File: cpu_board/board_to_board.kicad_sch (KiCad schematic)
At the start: 2 parts

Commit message: clean up board2board connector and organize TODOs
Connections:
- net BOOT_MODE1 is gone; now on net GPIO_SNVS_02: J?.21
- net DA_nRESET is gone; now on net GND: J?.59
- net ENET_RGMII_MDIO is gone; now on net GND: J?.46
- net ENET_RGMII_RXC is gone; now on net GPIO_DISP_B2_13: J?.78
- net ENET_RGMII_RXD0 is gone; now on net GPIO_DISP_B2_10: J?.70
- net ENET_RGMII_RXD1 is gone; now on net GPIO_DISP_B2_09: J?.68
- net ENET_RGMII_RXD2 is gone; now on net GPIO_DISP_B2_08: J?.66
- net ENET_RGMII_RXD3 is gone; now on net GND: J?.72
- net ENET_RGMII_RX_EN is gone; now on net GPIO_DISP_B2_12: J?.76
- net ENET_RGMII_TXC is gone; now on net GPIO_EMC_B2_10: J?.65
- net ENET_RGMII_TXD0 is gone; now on net GPIO_EMC_B2_09: J?.61
- net ENET_RGMII_TXD1 is gone; now on net GPIO_EMC_B2_08: J?.59
- net ENET_RGMII_TXD2 is gone; now on net GPIO_EMC_B2_07: J?.57
- net ENET_RGMII_TXD3 is gone; now on net GPIO_EMC_B2_06: J?.55
- net ENET_RGMII_TX_EN is gone; now on net GND: J?.63
- net GPIO_AD_24 is gone; now on net GND: J?.89
- net GPIO_AD_25 is gone; now on net GPIO_AD_27: J?.91
- net GPIO_EMC_B1_40 is gone; now on net VDD_3V3: J?.2
- net GPIO_EMC_B1_41 is gone; now on net GND: J?.22
- net GPIO_LPSR_10 is gone; now on net GND: J?.48
- net GPIO_LPSR_13 is gone; now on net GPIO_AD_07: J?.43
- net GPIO_LPSR_14 is gone; now on net GPIO_AD_06: J?.41
- net GPIO_LPSR_15 is gone; now on net GND: J?.39
- net GPIO_SD_B1_02 is gone; now on net GPIO_AD_34: J?.96
- net GPIO_SD_B2_04 is gone; now on net GND: J?.79
- net MIPI_DSI_D1_N is gone; now on net GND: J?.93
- net MIPI_DSI_D1_P is gone; now on net GND: J?.91
- net VDDA_1P0 is gone; now on net VDD_3V3: J?.5
- net VDD_LPSR_IN is gone; now on net VDD_1V8: J?.13
- net DAC_OUT: now also J?.20; no longer J?.95
- net DCDC_1V8_OUT: no longer J?.12
- net GND: now also J?.10, J?.100, J?.12, J?.18, J?.27, J?.29, J?.32, J?.34, J?.39, J?.58, J?.6, J?.60, J?.68, J?.75, J?.78, J?.88, J?.9; no longer J?.11, J?.12, J?.13, J?.15, J?.16, J?.17, J?.18, J?.20, J?.21, J?.23, J?.26, J?.28, J?.37, J?.38, J?.38, J?.4, J?.43, J?.48, J?.49, J?.53, J?.54, J?.57, J?.64, J?.67, J?.7, J?.70, J?.74, J?.76, J?.77, J?.8, J?.80, J?.82, J?.83, J?.84, J?.9, J?.90
- net GPIO_AD_00: now also J?.25; no longer J?.9
- net GPIO_AD_01: now also J?.27; no longer J?.7
- net GPIO_AD_02: now also J?.31; no longer J?.11
- net GPIO_AD_03: now also J?.33; no longer J?.5
- net GPIO_AD_06: no longer J?.10
- net GPIO_AD_07: no longer J?.14
- net GPIO_AD_11: now also J?.53; no longer J?.6
- net GPIO_AD_26: now also J?.87; no longer J?.3
- net GPIO_AD_27: no longer J?.1
- net GPIO_AD_28: now also J?.93; no longer J?.69
- net GPIO_AD_29: now also J?.95; no longer J?.71
- net GPIO_AD_30: now also J?.97; no longer J?.73
- net GPIO_AD_31: now also J?.90; no longer J?.75
- net GPIO_AD_32: now also J?.92; no longer J?.51
- net GPIO_AD_33: now also J?.94; no longer J?.52
- net GPIO_AD_34: no longer J?.93
- net GPIO_AD_35: now also J?.98; no longer J?.87
- net GPIO_DISP_B2_06: now also J?.62, J?.64; no longer J?.88
- net GPIO_DISP_B2_07: now also J?.64, J?.66; no longer J?.86
- net GPIO_DISP_B2_08: now also J?.70; no longer J?.52
- net GPIO_DISP_B2_09: now also J?.72; no longer J?.82
- net GPIO_DISP_B2_10: now also J?.74; no longer J?.58
- net GPIO_DISP_B2_11: now also J?.74, J?.76; no longer J?.60
- net GPIO_DISP_B2_12: now also J?.80; no longer J?.56
- net GPIO_DISP_B2_13: now also J?.82; no longer J?.54
- net GPIO_DISP_B2_14: now also J?.80, J?.84; no longer J?.62
- net GPIO_DISP_B2_15: now also J?.82, J?.86; no longer J?.50
- net GPIO_EMC_B2_00: now also J?.41; no longer J?.24
- net GPIO_EMC_B2_01: now also J?.43; no longer J?.47
- net GPIO_EMC_B2_02: now also J?.45; no longer J?.40
- net GPIO_EMC_B2_04: now also J?.49; no longer J?.66
- net GPIO_EMC_B2_05: now also J?.53; no longer J?.62
- net GPIO_EMC_B2_06: no longer J?.42
- net GPIO_EMC_B2_07: no longer J?.68
- net GPIO_EMC_B2_08: no longer J?.53
- net GPIO_EMC_B2_09: no longer J?.64
- net GPIO_EMC_B2_10: no longer J?.40
- net GPIO_LPSR_00: now also J?.1; no longer J?.97
- net GPIO_LPSR_01: now also J?.3; no longer J?.45
- net GPIO_LPSR_04: now also J?.11; no longer J?.15
- net GPIO_LPSR_05: now also J?.13; no longer J?.17
- net GPIO_LPSR_06: now also J?.15; no longer J?.72
- net GPIO_LPSR_07: now also J?.17; no longer J?.35, J?.74
- net GPIO_LPSR_09: now also J?.23; no longer J?.50
- net GPIO_SD_B1_00: now also J?.24; no longer J?.100
- net GPIO_SD_B1_01: now also J?.26; no longer J?.92
- net GPIO_SD_B1_03: now also J?.28; no longer J?.94
- net GPIO_SD_B1_04: now also J?.30; no longer J?.85
- net GPIO_SD_B1_05: now also J?.32; no longer J?.98
- net GPIO_SNVS_00: now also J?.17; no longer J?.31
- net GPIO_SNVS_02: no longer J?.80
- net GPIO_SNVS_03: now also J?.23; no longer J?.25
- net GPIO_SNVS_04: now also J?.25; no longer J?.58
- net GPIO_SNVS_05: now also J?.29; no longer J?.33
- net GPIO_SNVS_06: now also J?.31; no longer J?.78
- net GPIO_SNVS_07: now also J?.33; no longer J?.34
- net GPIO_SNVS_08: now also J?.35; no longer J?.56
- net GPIO_SNVS_09: now also J?.37; no longer J?.27
- net MCM_3V3: now also J?.4; no longer J?.6
- net MCM_3V3_SENSE: now also J?.2; no longer J?.8
- net ONOFF: now also J?.12; no longer J?.30
- net PMIC_ON_REQ: now also J?.18; no longer J?.29
- net PMIC_STBY_REQ: now also J?.14; no longer J?.32
- net VDD_1V8: now also J?.11, J?.15; no longer J?.47
- net VDD_1V8_SENSE: now also J?.9; no longer J?.45
- net VDD_3V3: now also J?.3, J?.4, J?.6, J?.7, J?.8; no longer J?.33, J?.83
- net VDD_3V3_SENSE: now also J?.1; no longer J?.31
- net WAKEUP: now also J?.16; no longer J?.36
- net BOOT_MODE0 renamed GPIO_SNVS_01
- net DA_GPIO0 renamed GPIO_AD_12
- net DA_GPIO2 renamed GPIO_AD_15
- net DA_GPIO3 renamed GPIO_AD_16
- net DA_GPIO4 renamed GPIO_AD_17
- net DA_nIRQ renamed GPIO_AD_14
- net ENET_RGMII_MDC renamed GPIO_DISP_B1_11
- net ETHPHY_RST_B renamed GPIO_DISP_B1_10
- net GPIO_LPSR_11 renamed USDHC2_CMD
- net GPIO_LPSR_12 renamed USDHC2_CLK
- net GPIO_SD_B2_00 renamed GPIO_AD_18
- net GPIO_SD_B2_01 renamed GPIO_AD_20
- net GPIO_SD_B2_02 renamed GPIO_AD_19
- net GPIO_SD_B2_03 renamed GPIO_AD_21
- net GPIO_SD_B2_05 renamed GPIO_AD_23
- net MIPI_DSI_CK_N renamed GPIO_EMC_B2_20
- net MIPI_DSI_CK_P renamed GPIO_EMC_B2_19
- net MIPI_DSI_D0_N renamed GPIO_EMC_B2_17
- net MIPI_DSI_D0_P renamed GPIO_EMC_B2_16
- net POR_B renamed GPIO_DISP_B2_04
- net GPIO_DISP_B2_04: now also J?.56
- new net BT_CFG_IO_EN: J?.37
- new net DCDC_1V8_OUT_SENSE: J?.8
- new net GPIO_AD_04: J?.35
- new net GPIO_AD_08: J?.45
- new net GPIO_AD_09: J?.47
- new net GPIO_AD_10: J?.51
- new net GPIO_AD_13: J?.57
- new net GPIO_AD_22: J?.83
- new net GPIO_DISP_B1_00: J?.20
- new net GPIO_DISP_B1_01: J?.22
- new net GPIO_DISP_B1_02: J?.24
- new net GPIO_DISP_B1_03: J?.26
- new net GPIO_DISP_B1_04: J?.28
- new net GPIO_DISP_B1_05: J?.30
- new net GPIO_DISP_B1_06: J?.34
- new net GPIO_DISP_B1_07: J?.36
- new net GPIO_DISP_B1_08: J?.38
- new net GPIO_DISP_B1_09: J?.40
- new net GPIO_DISP_B2_00: J?.48, J?.50
- new net GPIO_DISP_B2_01: J?.50, J?.52
- new net GPIO_DISP_B2_02: J?.52, J?.54
- new net GPIO_DISP_B2_03: J?.54, J?.56
- new net GPIO_DISP_B2_05: J?.58, J?.62
- new net GPIO_EMC_B2_03: J?.47
- new net GPIO_EMC_B2_11: J?.67
- new net GPIO_EMC_B2_12: J?.69
- new net GPIO_EMC_B2_13: J?.71
- new net GPIO_EMC_B2_14: J?.73
- new net GPIO_EMC_B2_15: J?.77
- new net GPIO_EMC_B2_18: J?.83
- new net GPIO_LPSR_02: J?.5
- new net GPIO_LPSR_03: J?.7
- new net GPIO_LPSR_08: J?.21
- new net LPUART1_RX_BOOT: J?.85
- new net USDHC2_DATA0: J?.42
- new net USDHC2_DATA1: J?.40
- new net USDHC2_DATA2: J?.38
- new net USDHC2_DATA3: J?.36
- new net VDD_SOC_IN: J?.16
- new net VDD_SOC_IN_SENSE: J?.14
- no-connect marks 22 -> 0
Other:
- note added: "1V8"
- note added: "GPIO_DISP_B1_06 to 11 & GPIO_DISP_B2_00 to 05 NOT FOR GENERAL USE Requires special consideration to avoid driving these at boot, or board may fail to boot"
- note removed: "1.8V System Power"
- note removed: "3.3V SYSTEM POWER"
- note removed: "5V SYSTEM POWER"
- note removed: "ADC"
- note removed: "CAMERA_INT"
- note removed: "CLK skew to be added by PHY"
- note removed: "DA_GPIO0"
- note removed: "DA_GPIO2"
- note removed: "DA_GPIO3"
- note removed: "DA_GPIO4"
- note removed: "DA_nRESET"
- note removed: "DMIC_DATA0"
- note removed: "DMIC_DATA1"
- note removed: "DMIC_DATA2"
- note removed: "DMIC_DATA3"
- note removed: "ENET"
- note removed: "FLEXPWM1_PWM0_A"
- note removed: "FLEXPWM1_PWM0_B"
- note removed: "FLEXPWM1_PWM1_A"
- note removed: "FLEXPWM1_PWM1_B"
- note removed: "FLEXPWM2_PWM1_A"
- note removed: "FLEXPWM2_PWM1_B"
- note removed: "GPIO_DISP_B1_06 to 11"
- note removed: "I2C1_SCL"
- note removed: "I2C5_SCL"
- note removed: "I2C5_SDA"
- note removed: "I2C6_SCL"
- note removed: "LPSPI6"
- note removed: "LPUART1 - NC to MCU at boot"
- note removed: "LPUART2"
- note removed: "LPUART6_RTS"
- note removed: "Length matched on mainboard"
- note removed: "MIPI"
- note removed: "NOT FOR GENERAL USE"
- note removed: "OUTPUT ONLY"
- note removed: "Odd pins 23-29 > SPARE PINS"
- note removed: "PMIC_ON_REQ"
- note removed: "Refer to datasheet for usage information"
- note removed: "Requires special consideration to avoid driving these at boot, or board may fail to boot"
- note removed: "SAI2"
- note removed: "SAI2_TX_DATA"
- note removed: "SENSE"
- note removed: "SYSTEM 1.8V"
- note removed: "USDHC2_CLK"
- note removed: "USDHC2_CMD"
- note removed: "USDHC2_DATA0"
- note removed: "USDHC2_DATA1"
- note removed: "USDHC2_DATA2"
- note removed: "USDHC2_DATA3"
- note removed: "USER_BUTTON"
- note removed: "USER_LED"
- note removed: "WIFI/BT"
- note removed: "WIFI_POWER_EN"

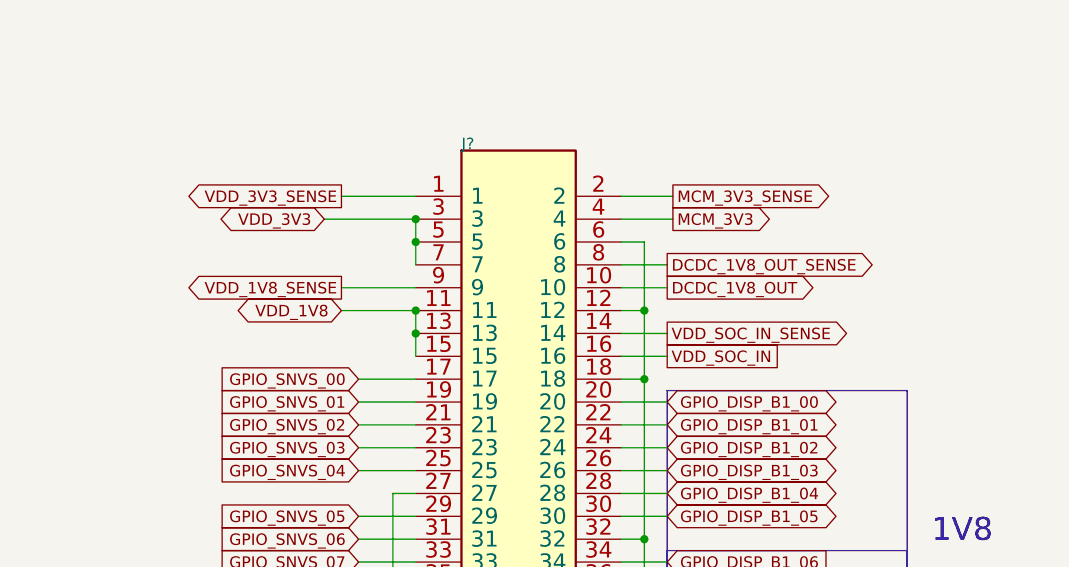
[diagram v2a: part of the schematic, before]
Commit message: clean up pwr slightly
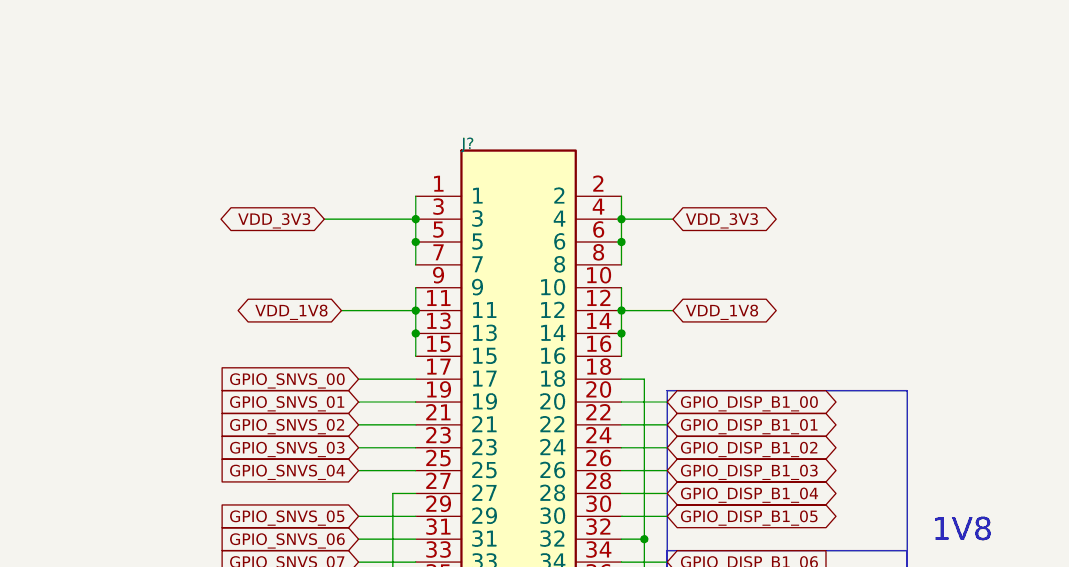
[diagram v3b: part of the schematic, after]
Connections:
- net DCDC_1V8_OUT is gone; now on net VDD_1V8: J?.10
- net DCDC_1V8_OUT_SENSE is gone; now on net VDD_3V3: J?.8
- net MCM_3V3 is gone; now on net VDD_3V3: J?.4
- net MCM_3V3_SENSE is gone; now on net VDD_3V3: J?.2
- net VDD_1V8_SENSE is gone; now on net VDD_1V8: J?.9
- net VDD_3V3_SENSE is gone; now on net VDD_3V3: J?.1
- net VDD_SOC_IN is gone; now on net VDD_1V8: J?.16
- net VDD_SOC_IN_SENSE is gone; now on net VDD_1V8: J?.14
- net GND: no longer J?.12, J?.6
- net VDD_1V8: now also J?.12
- net VDD_3V3: now also J?.6
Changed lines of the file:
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@@
   (junction (at 285.115 198.755) (diameter 0) (color 0 0 0 0)
   )
-  (junction (at 310.515 102.235) (diameter 0) (color 0 0 0 0)
-  )
-  (junction (at 310.515 94.615) (diameter 0) (color 0 0 0 0)
+  (junction (at 307.975 94.615) (diameter 0) (color 0 0 0 0)
   )
   (junction (at 285.115 97.155) (diameter 0) (color 0 0 0 0)
   )
+  (junction (at 307.975 86.995) (diameter 0) (color 0 0 0 0)
+  )
   (junction (at 310.515 137.795) (diameter 0) (color 0 0 0 0)
   )
@@
   (junction (at 99.06 184.15) (diameter 0) (color 0 0 0 0)
   )
+  (junction (at 307.975 97.155) (diameter 0) (color 0 0 0 0)
+  )
   (junction (at 99.06 196.85) (diameter 0) (color 0 0 0 0)
   )
@@
   (junction (at 310.515 201.295) (diameter 0) (color 0 0 0 0)
   )
+  (junction (at 307.975 84.455) (diameter 0) (color 0 0 0 0)
+  )
   (junction (at 127 156.21) (diameter 0) (color 0 0 0 0)
   )
@@
     (stroke (width 0) (type default))
   )
+  (wire (pts (xy 307.975 94.615) (xy 307.975 97.155))
+    (stroke (width 0) (type default))
+  )
   (wire (pts (xy 307.975 137.795) (xy 310.515 137.795))
     (stroke (width 0) (type default))
@@
     (stroke (width 0) (type default))
   )
-  (wire (pts (xy 310.515 94.615) (xy 310.515 102.235))
-    (stroke (width 0) (type default))
-  )
-  (wire (pts (xy 310.515 86.995) (xy 310.515 94.615))
-    (stroke (width 0) (type default))
-  )
   (wire (pts (xy 129.54 133.35) (xy 124.46 133.35))
     (stroke (width 0) (type default))
@@
     (stroke (width 0) (type default))
   )
-  (wire (pts (xy 307.975 94.615) (xy 310.515 94.615))
-    (stroke (width 0) (type default))
-  )
   (wire (pts (xy 99.06 95.25) (xy 99.06 107.95))
     (stroke (width 0) (type default))
@@
     (stroke (width 0) (type default))
   )
-  (wire (pts (xy 276.86 81.915) (xy 285.115 81.915))
-    (stroke (width 0) (type default))
-  )
   (wire (pts (xy 99.06 133.35) (xy 101.6 133.35))
     (stroke (width 0) (type default))
@@
     (stroke (width 0) (type default))
   )
-  (wire (pts (xy 313.055 97.155) (xy 307.975 97.155))
-    (stroke (width 0) (type default))
-  )
-  (wire (pts (xy 276.86 92.075) (xy 285.115 92.075))
-    (stroke (width 0) (type default))
-  )
   (wire (pts (xy 285.115 84.455) (xy 285.115 86.995))
     (stroke (width 0) (type default))
@@
     (stroke (width 0) (type default))
   )
-  (wire (pts (xy 313.69 81.915) (xy 307.975 81.915))
-    (stroke (width 0) (type default))
-  )
   (wire (pts (xy 313.055 168.275) (xy 307.975 168.275))
     (stroke (width 0) (type default))
@@
     (stroke (width 0) (type default))
   )
-  (wire (pts (xy 313.055 89.535) (xy 307.975 89.535))
-    (stroke (width 0) (type default))
-  )
   (wire (pts (xy 127 110.49) (xy 127 125.73))
     (stroke (width 0) (type default))
@@
     (stroke (width 0) (type default))
   )
+  (wire (pts (xy 307.975 86.995) (xy 307.975 89.535))
+    (stroke (width 0) (type default))
+  )
   (wire (pts (xy 127 95.25) (xy 127 110.49))
     (stroke (width 0) (type default))
@@
     (stroke (width 0) (type default))
   )
+  (wire (pts (xy 307.975 97.155) (xy 307.975 99.695))
+    (stroke (width 0) (type default))
+  )
   (wire (pts (xy 129.54 148.59) (xy 124.46 148.59))
     (stroke (width 0) (type default))
@@
     (stroke (width 0) (type default))
   )
-  (wire (pts (xy 307.975 86.995) (xy 310.515 86.995))
-    (stroke (width 0) (type default))
-  )
   (wire (pts (xy 313.055 178.435) (xy 307.975 178.435))
     (stroke (width 0) (type default))
@@
     (stroke (width 0) (type default))
   )
+  (wire (pts (xy 285.115 92.075) (xy 285.115 94.615))
+    (stroke (width 0) (type default))
+  )
   (wire (pts (xy 285.115 193.675) (xy 285.115 196.215))
     (stroke (width 0) (type default))
@@
     (stroke (width 0) (type default))
   )
-  (wire (pts (xy 313.055 99.695) (xy 307.975 99.695))
-    (stroke (width 0) (type default))
-  )
   (wire (pts (xy 129.54 207.01) (xy 124.46 207.01))
     (stroke (width 0) (type default))
@@
     (stroke (width 0) (type default))
   )
+  (wire (pts (xy 307.975 92.075) (xy 307.975 94.615))
+    (stroke (width 0) (type default))
+  )
   (wire (pts (xy 124.46 90.17) (xy 124.46 92.71))
     (stroke (width 0) (type default))
@@
     (stroke (width 0) (type default))
   )
+  (wire (pts (xy 307.975 84.455) (xy 307.975 86.995))
+    (stroke (width 0) (type default))
+  )
   (wire (pts (xy 129.54 118.11) (xy 124.46 118.11))
     (stroke (width 0) (type default))
@@
     (stroke (width 0) (type default))
   )
+  (wire (pts (xy 307.975 94.615) (xy 313.69 94.615))
+    (stroke (width 0) (type default))
+  )
   (wire (pts (xy 313.055 180.975) (xy 307.975 180.975))
     (stroke (width 0) (type default))
@@
     (stroke (width 0) (type default))
   )
-  (wire (pts (xy 313.055 92.075) (xy 307.975 92.075))
-    (stroke (width 0) (type default))
-  )
   (wire (pts (xy 129.54 113.03) (xy 124.46 113.03))
     (stroke (width 0) (type default))
   )
+  (wire (pts (xy 285.115 81.915) (xy 285.115 84.455))
+    (stroke (width 0) (type default))
+  )
   (wire (pts (xy 99.06 217.17) (xy 99.06 214.63))
     (stroke (width 0) (type default))
@@
   )
   (wire (pts (xy 313.69 84.455) (xy 307.975 84.455))
+    (stroke (width 0) (type default))
+  )
+  (wire (pts (xy 307.975 81.915) (xy 307.975 84.455))
     (stroke (width 0) (type default))
   )
@@
     )
   )
-  (global_label "MCM_3V3_SENSE" (shape output) (at 313.69 81.915 0) (fields_autoplaced)
-    (effects (font (size 1.27 1.27)) (justify left))
-    (property "Intersheetrefs" "${INTERSHEET_REFS}" (at 332.3383 81.915 0)
-      (effects (font (size 1.27 1.27)) (justify left) hide)
-    )
-  )
   (global_label "GPIO_AD_13" (shape bidirectional) (at 96.52 156.21 180) (fields_autoplaced)
     (effects (font (size 1.27 1.27)) (justify right))
@@
     )
   )
-  (global_label "VDD_1V8_SENSE" (shape output) (at 276.86 92.075 180) (fields_autoplaced)
-    (effects (font (size 1.27 1.27)) (justify right))
-    (property "Intersheetrefs" "${INTERSHEET_REFS}" (at 258.7559 92.075 0)
-      (effects (font (size 1.27 1.27)) (justify right) hide)
-    )
-  )
   (global_label "GPIO_DISP_B2_10" (shape bidirectional) (at 313.055 168.275 0) (fields_autoplaced)
     (effects (font (size 1.27 1.27)) (justify left))
@@
     )
   )
-  (global_label "VDD_3V3_SENSE" (shape output) (at 276.86 81.915 180) (fields_autoplaced)
-    (effects (font (size 1.27 1.27)) (justify right))
-    (property "Intersheetrefs" "${INTERSHEET_REFS}" (at 258.7559 81.915 0)
-      (effects (font (size 1.27 1.27)) (justify right) hide)
-    )
-  )
   (global_label "GPIO_AD_00" (shape bidirectional) (at 96.52 115.57 180) (fields_autoplaced)
     (effects (font (size 1.27 1.27)) (justify right))
@@
     )
   )
-  (global_label "VDD_SOC_IN_SENSE" (shape output) (at 313.055 97.155 0) (fields_autoplaced)
-    (effects (font (size 1.27 1.27)) (justify left))
-    (property "Intersheetrefs" "${INTERSHEET_REFS}" (at 334.3644 97.155 0)
-      (effects (font (size 1.27 1.27)) (justify left) hide)
-    )
-  )
   (global_label "GPIO_DISP_B1_07" (shape input) (at 313.055 125.095 0) (fields_autoplaced)
     (effects (font (size 1.27 1.27)) (justify left))
@@
     )
   )
+  (global_label "VDD_1V8" (shape bidirectional) (at 313.69 94.615 0) (fields_autoplaced)
+    (effects (font (size 1.27 1.27)) (justify left))
+    (property "Intersheetrefs" "${INTERSHEET_REFS}" (at 325.8903 94.615 0)
+      (effects (font (size 1.27 1.27)) (justify left) hide)
+    )
+  )
   (global_label "GPIO_SNVS_03" (shape input) (at 278.765 109.855 180) (fields_autoplaced)
     (effects (font (size 1.27 1.27)) (justify right))
@@
     )
   )
+  (global_label "VDD_3V3" (shape bidirectional) (at 313.69 84.455 0) (fields_autoplaced)
+    (effects (font (size 1.27 1.27)) (justify left))
+    (property "Intersheetrefs" "${INTERSHEET_REFS}" (at 325.8903 84.455 0)
+      (effects (font (size 1.27 1.27)) (justify left) hide)
+    )
+  )
   (global_label "GPIO_DISP_B2_01" (shape bidirectional) (at 129.54 148.59 0) (fields_autoplaced)
     (effects (font (size 1.27 1.27)) (justify left))
@@
     )
   )
-  (global_label "MCM_3V3" (shape output) (at 313.69 84.455 0) (fields_autoplaced)
-    (effects (font (size 1.27 1.27)) (justify left))
-    (property "Intersheetrefs" "${INTERSHEET_REFS}" (at 325.3232 84.455 0)
-      (effects (font (size 1.27 1.27)) (justify left) hide)
-    )
-  )
   (global_label "GPIO_DISP_B2_05" (shape bidirectional) (at 313.055 153.035 0) (fields_autoplaced)
     (effects (font (size 1.27 1.27)) (justify left))
@@
     )
   )
-  (global_label "DCDC_1V8_OUT_SENSE" (shape output) (at 313.055 89.535 0) (fields_autoplaced)
-    (effects (font (size 1.27 1.27)) (justify left))
-    (property "Intersheetrefs" "${INTERSHEET_REFS}" (at 337.2067 89.535 0)
-      (effects (font (size 1.27 1.27)) (justify left) hide)
-    )
-  )
-  (global_label "VDD_SOC_IN" (shape passive) (at 313.055 99.695 0) (fields_autoplaced)
-    (effects (font (size 1.27 1.27)) (justify left))
-    (property "Intersheetrefs" "${INTERSHEET_REFS}" (at 326.238 99.695 0)
-      (effects (font (size 1.27 1.27)) (justify left) hide)
-    )
-  )
   (global_label "GPIO_DISP_B2_08" (shape bidirectional) (at 313.055 163.195 0) (fields_autoplaced)
     (effects (font (size 1.27 1.27)) (justify left))
@@
     )
   )
-  (global_label "DCDC_1V8_OUT" (shape output) (at 313.055 92.075 0) (fields_autoplaced)
-    (effects (font (size 1.27 1.27)) (justify left))
-    (property "Intersheetrefs" "${INTERSHEET_REFS}" (at 330.1916 92.075 0)
-      (effects (font (size 1.27 1.27)) (justify left) hide)
-    )
-  )
